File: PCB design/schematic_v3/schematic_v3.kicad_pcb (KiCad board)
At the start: 4 copper layers, 108 parts, among them IC1 LAN9252, J1 Conn_01x04_Pin, J2 connection_moteur, J3 Conn_01x05_Pin, J4 Conn_01x03_Pin, J5 Conn_01x02_Pin, Q1 AO3400A, U1 HX1188NL, U2 SP3485CN, U3 24FC512-I/ST, U4 LMR14030SQDPRTQ1, U5 STM32F446RETx, U7 AP63203WU, Y1 25MHz, Y2 8MHz

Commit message: pcb updated
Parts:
- removed C50, C51, C57: 100n, Capacitor_SMD:C_0603_1608Metric
- removed C52: 270p, Capacitor_SMD:C_0603_1608Metric
- removed C53, C55: 27u, Capacitor_SMD:C_1206_3216Metric
- removed C56: 10u, Capacitor_SMD:C_1206_3216Metric
- removed C58, C59: 22u, Capacitor_SMD:C_1206_3216Metric
- removed L3: 6.8u, Inductor_SMD:L_Bourns-SRN4018
- removed U7: AP63203WU, Package_TO_SOT_SMD:TSOT-23-6
- added C23: 18p, Capacitor_SMD:C_0603_1608Metric, F.Cu at (160.4, 90.1)
- added C24: 100n, Capacitor_SMD:C_0603_1608Metric, F.Cu at (149.4, 106.0)
- added C25: 100n, Capacitor_SMD:C_0603_1608Metric, F.Cu at (159.1, 109.5)
- added C31: 100n, Capacitor_SMD:C_0603_1608Metric, F.Cu at (142.1, 105.9)
- added C32: 20p, Capacitor_SMD:C_0603_1608Metric, F.Cu at (135.9, 105.9)
- added C34: 100n, Capacitor_SMD:C_0603_1608Metric, B.Cu at (176.7, 102.3)
- added C36: 1u, Capacitor_SMD:C_0603_1608Metric, F.Cu at (133.8, 89.5)
- added C37: 4.7u, Capacitor_SMD:C_0603_1608Metric, F.Cu at (147.2, 95.6)
- added C49: 22u, Capacitor_SMD:C_1206_3216Metric, B.Cu at (164.6, 83.0)
- added F1: 2920L150_60MR, footprints:2920L150_60MR, B.Cu at (176.4, 110.1)
- added H1: MountingHole, MountingHole:MountingHole_3.2mm_M3_Pad_Via, F.Cu at (127.5, 80.2)
- added H2: MountingHole, MountingHole:MountingHole_3.2mm_M3_Pad_Via, F.Cu at (186.5, 115.2)
- added H3: MountingHole, MountingHole:MountingHole_3.2mm_M3_Pad_Via, F.Cu at (127.5, 115.2)
- added H4: MountingHole, MountingHole:MountingHole_3.2mm_M3_Pad_Via, F.Cu at (186.5, 80.2)
- added L2: 6.8u, Inductor_SMD:L_Bourns-SRN4018, B.Cu at (167.5, 89.5)
- added U6: AP63203WU, Package_TO_SOT_SMD:TSOT-23-6, B.Cu at (173.9, 88.5)
- C1, C11, C13, C15, C16, C17, C21, C28, C35: value 0.1u -> 100n
- C10: value 47u -> 1n; footprint Capacitor_SMD:CP_Elec_5x5.4 -> Capacitor_SMD:C_0603_1608Metric; moved to F.Cu
- C18: value 47u -> 1u; footprint Capacitor_SMD:CP_Elec_5x5.4 -> Capacitor_SMD:C_0603_1608Metric; moved to F.Cu
- C20: value 1u -> 100n
- C22: value 0.1u -> 18p
- C26: value 18p -> 47u; footprint Capacitor_SMD:C_0603_1608Metric -> Capacitor_SMD:CP_Elec_5x5.4; moved to B.Cu
- C27: value 18p -> 100n
- C30: value 0.1u -> 100n; footprint Capacitor_SMD:C_0603_1608Metric -> Capacitor_SMD:C_1206_3216Metric; moved to B.Cu
- C33: value 0.1u -> 20p
- C38: footprint Capacitor_SMD:C_1206_3216Metric -> Capacitor_SMD:C_0603_1608Metric; moved to F.Cu
- C39: value 100n -> 10u; footprint Capacitor_SMD:C_0603_1608Metric -> Capacitor_SMD:C_1206_3216Metric; moved to B.Cu
- C40, C41: value 20p -> 100n
- C44: value 1u -> 270p; moved to B.Cu
- C45: value 4.7u -> 100n; moved to B.Cu
- C46, C48: value 100n -> 27u; footprint Capacitor_SMD:C_0603_1608Metric -> Capacitor_SMD:C_1206_3216Metric; moved to B.Cu
- C47: value 100n -> 22u; footprint Capacitor_SMD:C_0603_1608Metric -> Capacitor_SMD:C_1206_3216Metric; moved to B.Cu
- C5: value 10p -> 100n; moved to B.Cu
- C6: value 0.1u -> 10p; moved to F.Cu
- C8: moved to F.Cu
- C9: value 1n -> 47u; footprint Capacitor_SMD:C_0603_1608Metric -> Capacitor_SMD:CP_Elec_5x5.4
- J2: value connection_moteur -> Conn_01x02_Pin; footprint Connector_JST:JST_EH_B4B-EH-A_1x04_P2.50mm_Vertical -> Connector_JST:JST_EH_B2B-EH-A_1x02_P2.50mm_Vertical
- J3: value Conn_01x05_Pin -> connection_moteur; footprint Connector_PinHeader_1.27mm:PinHeader_1x05_P1.27mm_Vertical -> Connector_JST:JST_EH_B4B-EH-A_1x04_P2.50mm_Vertical
- J4: value Conn_01x03_Pin -> Conn_01x05_Pin; footprint Connector_PinHeader_1.27mm:PinHeader_1x03_P1.27mm_Vertical -> Connector_PinHeader_1.27mm:PinHeader_1x05_P1.27mm_Vertical
- J5: value Conn_01x02_Pin -> Conn_01x03_Pin; footprint Connector_JST:JST_EH_B2B-EH-A_1x02_P2.50mm_Vertical -> Connector_JST:JST_EH_B3B-EH-A_1x03_P2.50mm_Vertical; moved to F.Cu
- R1: value 49.9 -> 47k; moved to B.Cu
- R16: value 12.1k -> 12k
- R2: value 47k -> 49.9; moved to F.Cu
- S1: value TS40-66-43-BK-260-SMT-TR -> B3U-1100PM; footprint footprints:TS40-66-43-BK-260-SMT-TR -> footprints:B3U1100PM
- U1: value HX1188NL -> SP3485CN; footprint footprints:HX1188NL -> Package_SO:SOIC-8_3.9x4.9mm_P1.27mm; moved to B.Cu
- U2: value SP3485CN -> HX1188NL; footprint Package_SO:SOIC-8_3.9x4.9mm_P1.27mm -> footprints:HX1188NL; moved to F.Cu
- moved Q1 100.9 mm to (132.5, 105.4), turned to -90 degrees
- moved R14 98.1 mm to (132.5, 100.8), turned to 180 degrees
- moved R13 98.1 mm to (132.5, 102.3), turned to 0 degrees
- moved J5 98.0 mm to (134.8, 116.2), turned to 0 degrees
- moved C38 92.0 mm to (149.5, 102.5), turned to 180 degrees
- moved D1 91.7 mm to (138.1, 110.9), turned to 180 degrees
- moved R3 90.5 mm to (137.4, 96.5), turned to 180 degrees
- moved R10 86.6 mm to (148.0, 97.0), turned to 90 degrees
- moved R9 86.4 mm to (148.5, 99.7), turned to 180 degrees
- moved R8 85.8 mm to (146.0, 93.5), turned to 180 degrees
- moved D3 81.8 mm to (149.3, 110.9), turned to 180 degrees
- moved L1 79.1 mm to (162.1, 111.5), turned to -90 degrees
- moved J2 78.6 mm to (177.3, 116.2), turned to 0 degrees
- moved C18 74.7 mm to (165.6, 106.2), turned to 90 degrees
- moved R24 66.3 mm to (171.6, 93.8), turned to 90 degrees
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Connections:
- net Net-(IC1-RBIAS) renamed /RBIAS
- net Net-(IC1-VDD33BIAS) renamed /VDD33BIAS
- net Net-(Q1-G) renamed /GATE
- net Net-(U3-A0) renamed /AX
- net Net-(U4-PGOOD) renamed /PGOOD
- net Net-(U4-RT_SYNC) renamed /RT_SYNC
- net Net-(U5-BOOT0) renamed /BOOT0
- net Net-(U5-PA5) renamed /PA5
- net Net-(U5-PA6) renamed /PA6
- net Net-(U5-PA7) renamed /PA7
- C10 pad 1: +12V -> /CMT
- C18 pad 1: Net-(D2-K) -> /VDD33TXRX1
- C19 pad 1: /VDD33TXRX1 -> /VDD33TXRX2
- C20 pad 1: /VDD33TXRX2 -> /VDDCR
- C21 pad 1: /VDDCR -> +3.3V
- C22 pad 1: +3.3V -> GND
- C22 pad 2: GND -> Net-(C22-Pad2)
- C26 pad 1: GND -> /VIN
- C26 pad 2: Net-(C26-Pad2) -> GND
- C27 pad 1: GND -> /VDD12TX1
- C27 pad 2: /OSCO -> GND
- C28 pad 1: +3.3V -> /VDD12TX1
- C29 pad 1: Net-(D2-K) -> /VIN
- C30 pad 1: GND -> /VIN
- C30 pad 2: +3.3V -> GND
- C33 pad 1: /VDD12TX1 -> GND
- C33 pad 2: GND -> /PH1
- C35 pad 1: /VDD12TX1 -> GND
- C35 pad 2: GND -> /NRST
- C38 pad 1: Net-(D2-K) -> +3.3V
- C38 pad 2: GND -> /VDD19
- C39 pad 1: /AVDD -> +12V
- C40 pad 1: GND -> +3.3V
- C40 pad 2: Net-(U5-PH0) -> /VDD32
- C41 pad 1: GND -> +3.3V
- C41 pad 2: Net-(U5-PH1) -> /VDD48
- C42 pad 1: Net-(U4-SS) -> /BOOT
- C42 pad 2: GND -> /SW
- C43 pad 1: GND -> +3.3V
- C43 pad 2: /NRST -> /VDD64
- C44 pad 1: GND -> +12V
- C44 pad 2: +3.3V -> /FB
- C45 pad 1: Net-(U5-VCAP_1) -> /SW
- C45 pad 2: GND -> /BST
- C46 pad 1: +3.3V -> +12V
- C46 pad 2: Net-(C46-Pad2) -> GND
- C47 pad 2: Net-(C47-Pad2) -> GND
- C48 pad 1: +3.3V -> +12V
- C48 pad 2: Net-(C48-Pad2) -> GND
- C5 pad 1: /RXA_N -> +3.3V
- C6 pad 1: +3.3V -> /RXA_N
- C7 pad 1: Net-(U1-RCT) -> /TCT
- C9 pad 1: Net-(C9-Pad1) -> +12V
- D1 pad 1: Net-(D1-K) -> +12V
- D1 pad 2: +12V -> /DRAIN
- D2 pad 1: Net-(D2-K) -> /VIN
- D2 pad 2: +36V -> Net-(D2-A)
- D3 pad 1: Net-(D3-K) -> /SW
- J1 pad 1: Net-(J1-Pin_1) -> /RX_N
- J1 pad 2: Net-(J1-Pin_2) -> /RX_P
- J1 pad 3: Net-(J1-Pin_3) -> /TX_N
- J1 pad 4: Net-(J1-Pin_4) -> /TX_P
- J2 pad 1: Net-(D1-K) -> GND
- J2 pad 2: +12V -> +36V
- J3 pad 1: /SWDIO -> /DRAIN
- J3 pad 2: /SWCLK -> +12V
- J3 pad 3: GND -> /DATA+
- J3 pad 4: +3.3V -> /DATA-
- J4 pad 1: Net-(J4-Pin_1) -> /SWDIO
- J4 pad 2: Net-(J4-Pin_2) -> /SWCLK
- J4 pad 3: Net-(J4-Pin_3) -> GND
- J5 pad 1: GND -> /PA1
- J5 pad 2: +36V -> /PA0
- L1 pad 1: Net-(D3-K) -> /SW
- Q1 pad 3: Net-(D1-K) -> /DRAIN
- R1 pad 1: /VDD33TXRX1 -> GND
- R1 pad 2: /TXA_P -> /RS485_MODE
- R10 pad 1: Net-(J2-Pin_4) -> /DATA-
- R10 pad 2: Net-(J2-Pin_3) -> /DATA+
- R11 pad 1: Net-(C9-Pad1) -> /CMT
- R11 pad 2: Net-(R11-Pad2) -> /CMT1
- R12 pad 1: Net-(C9-Pad1) -> /CMT
- R12 pad 2: Net-(R12-Pad2) -> /CMT2
- R2 pad 1: GND -> /VDD33TXRX1
- R2 pad 2: /RS485_MODE -> /TXA_P
- R20 pad 2: Net-(C26-Pad2) -> Net-(C22-Pad2)
- R23 pad 1: Net-(D2-K) -> /VIN
- R28 pad 2: Net-(U4-FB) -> /FB
- R29 pad 1: Net-(U4-FB) -> /FB
- R3 pad 1: Net-(U2-DE) -> /DE/RE
- R7 pad 2: Net-(U1-RCT) -> /TCT
- R8 pad 1: Net-(J2-Pin_3) -> /DATA+
- R9 pad 2: Net-(J2-Pin_4) -> /DATA-
- S1 pad 1: GND -> /NRST
- S1 pad 3: /NRST -> GND
- U1 pad 1: /TXA_P -> /RO
- U1 pad 2: Net-(U1-RCT) -> /DE/RE
- U1 pad 3: /TXA_N -> /DE/RE
- U1 pad 4: unconnected-(U1-NC-Pad4) -> /DI
- U1 pad 5: unconnected-(U1-NC-Pad5) -> GND
- U1 pad 6: /RXA_P -> /DATA+
- U1 pad 7: Net-(U1-RCT) -> /DATA-
- U1 pad 8: /RXA_N -> +3.3V
- U2 pad 1: /RO -> /TXA_P
- U2 pad 2: Net-(U2-DE) -> /TCT
- U2 pad 3: Net-(U2-DE) -> /TXA_N
- U2 pad 4: /DI -> unconnected-(U2-NC-Pad4)
- U2 pad 5: GND -> unconnected-(U2-NC-Pad5)
- U2 pad 6: Net-(J2-Pin_3) -> /RXA_P
- U2 pad 7: Net-(J2-Pin_4) -> /TCT
- U2 pad 8: +3.3V -> /RXA_N
- U4 pad 1: Net-(U4-BOOT) -> /BOOT
- U4 pad 10: Net-(D3-K) -> /SW
- U4 pad 2: Net-(D2-K) -> /VIN
- U4 pad 3: Net-(D2-K) -> /VIN
- U4 pad 4: Net-(D2-K) -> /VIN
- U4 pad 6: Net-(U4-SS) -> /SS
- U4 pad 7: Net-(U4-FB) -> /FB
- U5 pad 14: Net-(J4-Pin_2) -> /PA0
- U5 pad 15: Net-(J4-Pin_3) -> /PA1
- U5 pad 19: Net-(C46-Pad2) -> /VDD19
- U5 pad 20: Net-(J4-Pin_1) -> /PA4
- U5 pad 30: Net-(U5-VCAP_1) -> /VCAP_1
- U5 pad 32: Net-(C47-Pad2) -> /VDD32
- U5 pad 48: Net-(C48-Pad2) -> /VDD48
- U5 pad 5: Net-(U5-PH0) -> /PH0
- U5 pad 6: Net-(U5-PH1) -> /PH1
- U5 pad 64: Net-(C51-Pad2) -> /VDD64
- Y1 pad 2: Net-(C26-Pad2) -> Net-(C22-Pad2)
- Y2 pad 1: Net-(U5-PH1) -> /PH1
- Y2 pad 2: Net-(U5-PH0) -> /PH0
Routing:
- net GND: track 0.00 -> 132.1 mm, vias 0 -> 78
- net +3.3V: track 0.00 -> 81.0 mm, vias 0 -> 31
- net /DRAIN: track 0.00 -> 80.6 mm
- net /DATA+: track 0.00 -> 72.4 mm
- net /DATA-: track 0.00 -> 58.0 mm
- net +12V: track 18.4 -> 60.0 mm, vias 0 -> 7
- net /RST#: track 0.00 -> 37.7 mm, vias 0 -> 2
- net /SCS#: track 0.00 -> 36.7 mm, vias 0 -> 2
- net /SW: track 0.00 -> 35.8 mm
- net /IRQ: track 0.00 -> 30.1 mm, vias 0 -> 2
- net /RXA_N: track 45.2 -> 15.5 mm, vias 0 -> 2
- net /PA0: track 0.00 -> 26.1 mm
- net /PA1: track 0.00 -> 26.0 mm
- net /PA4: track 0.00 -> 24.5 mm
- net /TX_N: track 0.00 -> 24.4 mm
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- added copper zone on B.Cu, net +12V
- added copper zone on In2.Cu, net +12V
- added copper zone on B.Cu, net +3.3V
- added copper zone on F.Cu, net +3.3V
- added copper zone on In2.Cu, net +3.3V
- added copper zone on B.Cu, net /GATE
- added copper zone on F.Cu, net /VDDCR
- added copper zone on B.Cu, net GND
- added copper zone on F.Cu, net GND
- added copper zone on In1.Cu, net GND
- added copper zone on In2.Cu, net GND
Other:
- board outline added: 67 x 43 mm
- board text added: "+3.3V"
- board text added: "+36V|GND"
- board text added: "ECAT"
- board text added: "GND"
- board text added: "GND|12V|D+|D-"
- board text added: "GPIO PINS"
- board text added: "Heemskerk Innovative Technology Robot Gripper Controller"
- board text added: "NRST"
- board text added: "PA0"
- board text added: "PA1"
- board text added: "PA4"
- board text added: "PWR"
- board text added: "RS485"
- board text added: "RX_N|RX_P|TX_N|TX_P"
- board text added: "SWCLK"
- board text added: "SWDIO"
- board text removed: "Module RS485"
- board text removed: "Zone EtherCAT (LAN9252)"
- board text removed: "Zone MCU"
- board text removed: "Zone d'alimentation"
- board text removed: "Zone entrée robot"

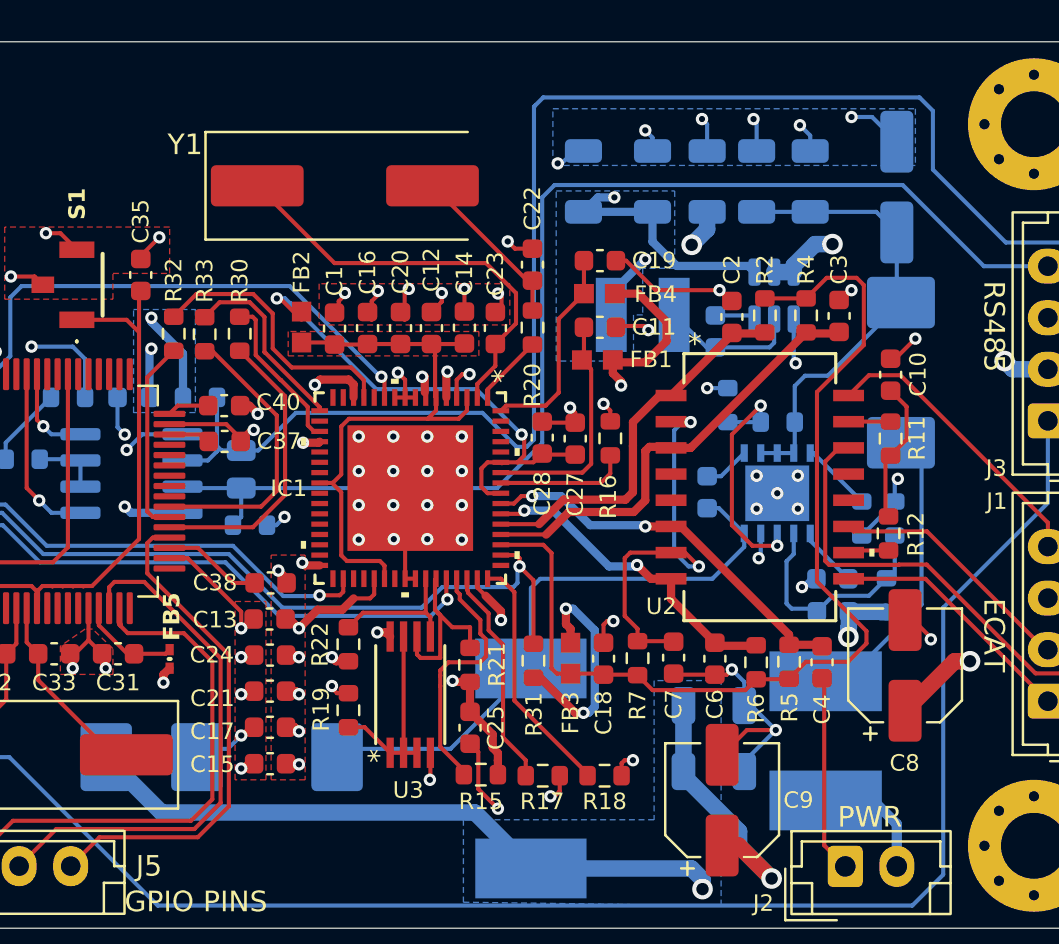
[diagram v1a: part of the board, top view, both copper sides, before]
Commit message: 1KHz ecat communication frequency done
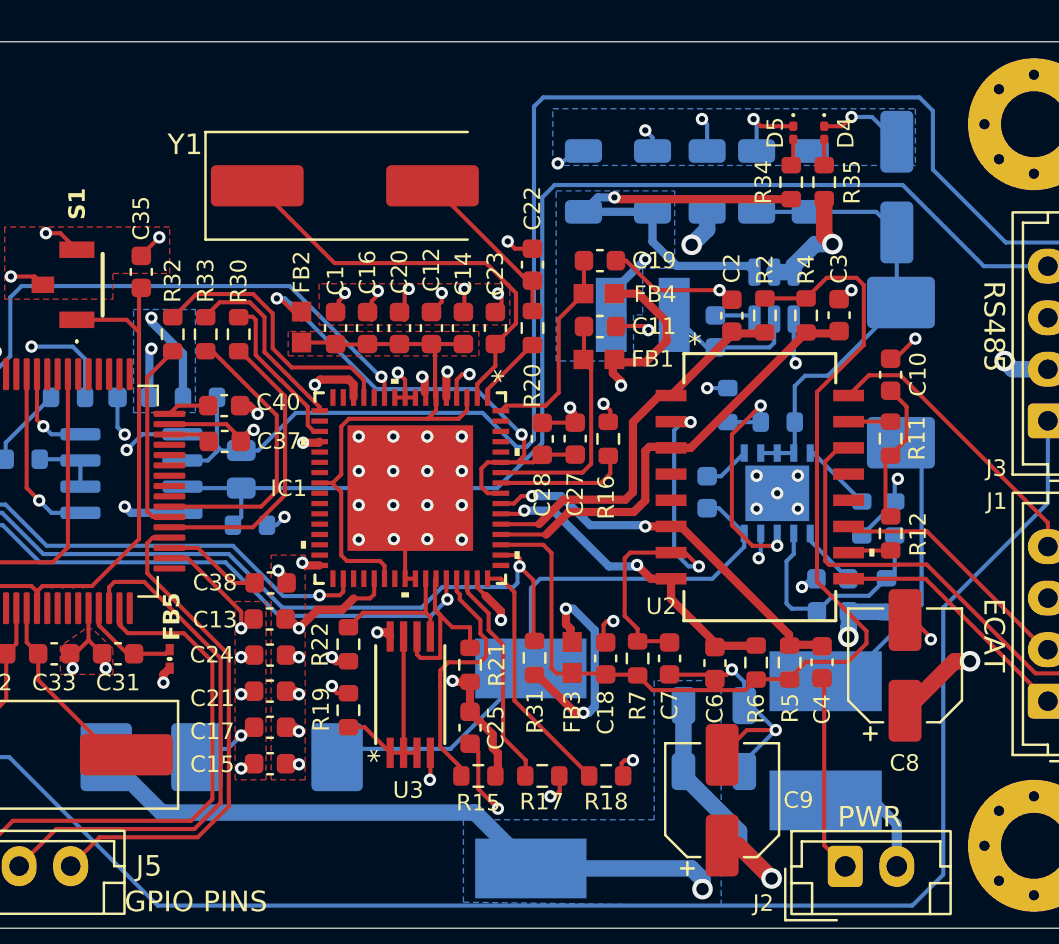
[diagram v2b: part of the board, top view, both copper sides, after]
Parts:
- added D4: LED_Small, LED_SMD:LED_0201_0603Metric, F.Cu at (176.3, 80.6)
- added D5: LED_Small, LED_SMD:LED_0201_0603Metric, F.Cu at (174.8, 80.6)
- added R34: 1k, Resistor_SMD:R_0603_1608Metric, F.Cu at (174.7, 83.0)
- added R35: 3.3k, Resistor_SMD:R_0603_1608Metric, F.Cu at (176.3, 83.0)
- moved C6 0.21 mm to (171.0, 106.4)
- moved C7 0.20 mm to (168.8, 106.1)
- moved C35 0.15 mm to (143.2, 87.4)
- moved R31 0.15 mm to (162.3, 106.1)
- moved R15 0.14 mm to (159.6, 111.8)
- moved C18 0.10 mm to (165.7, 106.1)
- moved R16 0.10 mm to (165.9, 95.5)
- moved R12 0.10 mm to (179.6, 100.1)
- moved FB3 0.09 mm to (164.1, 106.1)
- moved FB1 0.08 mm to (165.4, 91.6)
- moved R18 0.08 mm to (165.8, 111.8)
- moved C2 0.06 mm to (171.8, 89.5)
- moved C28 0.06 mm to (162.7, 95.5)
- moved R32 0.06 mm to (144.7, 90.4)
- moved C1 0.06 mm to (152.6, 90.1)
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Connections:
- C42 pad 2: /SW -> Net-(D3-K)
- D3 pad 1: /SW -> Net-(D3-K)
- L1 pad 1: /SW -> Net-(D3-K)
- U4 pad 10: /SW -> Net-(D3-K)
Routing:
- net /SW: track 35.8 -> 6.75 mm
- net Net-(D3-K): track 0.00 -> 29.1 mm
- net +3.3V: track 81.0 -> 89.7 mm
- net +12V: track 60.0 -> 62.4 mm
- net GND: track 132.1 -> 134.2 mm, vias 78 -> 77
- net Net-(D5-A): track 0.00 -> 1.25 mm
- net Net-(D4-A): track 0.00 -> 1.25 mm

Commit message: PCB ordered
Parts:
- removed Q1: AO3400A, Package_TO_SOT_SMD:SOT-23
- removed U2: HX1188NL, footprints:HX1188NL
- removed Y1: 25MHz, Crystal:Crystal_SMD_HC49-SD
- added C50: 10u, Capacitor_SMD:C_1206_3216Metric, B.Cu at (175.7, 88.6)
- added C51: 56p, Capacitor_SMD:C_0603_1608Metric, B.Cu at (168.7, 84.8)
- added D6: LED_Small, LED_SMD:LED_0603_1608Metric, F.Cu at (147.4, 98.7)
- added D7: LED_Small, LED_SMD:LED_0603_1608Metric, F.Cu at (132.1, 93.1)
- added D8: PRTR5V0U2X, Package_TO_SOT_SMD:SOT-143, F.Cu at (144.6, 116.1)
- added IC2: SON50P300X300X100-11N-D, footprints:MP5000ADQ-LF-Z, B.Cu at (171.8, 83.0)
- added R36: 1k, Resistor_SMD:R_0603_1608Metric, F.Cu at (131.4, 89.3)
- added R37: 10k, Resistor_SMD:R_0603_1608Metric, F.Cu at (135.5, 86.4)
- added R38: 1k, Resistor_SMD:R_0603_1608Metric, F.Cu at (147.3, 97.1)
- added R39: 1k, Resistor_SMD:R_0603_1608Metric, F.Cu at (132.6, 91.6)
- added R40: 1k, Resistor_SMD:R_0603_1608Metric, F.Cu at (140.2, 113.2)
- added R41: 1k, Resistor_SMD:R_0603_1608Metric, F.Cu at (136.5, 112.4)
- added R42: 1k, Resistor_SMD:R_0603_1608Metric, F.Cu at (134.9, 112.4)
- added R43: 10k, Resistor_SMD:R_0603_1608Metric, F.Cu at (142.9, 109.8)
- added R44: 10k, Resistor_SMD:R_0603_1608Metric, F.Cu at (144.5, 109.8)
- added R45: 10k, Resistor_SMD:R_0603_1608Metric, F.Cu at (146.1, 109.8)
- added R46: 100, Resistor_SMD:R_0603_1608Metric, F.Cu at (178.4, 85.4)
- added R47: 100, Resistor_SMD:R_0603_1608Metric, F.Cu at (165.8, 82.0)
- added S2: B3U-1100PM, footprints:B3U1100PM, F.Cu at (128.1, 94.9)
- added T1: 7490100110A, footprints:7490100110A, F.Cu at (176.0, 98.5)
- added TP1: TestPoint, TestPoint:TestPoint_Pad_D1.0mm, F.Cu at (176.0, 108.4)
- added TP2: TestPoint, TestPoint:TestPoint_Pad_D1.0mm, F.Cu at (180.2, 83.6)
- added TP3: TestPoint, TestPoint:TestPoint_Pad_D1.0mm, F.Cu at (165.6, 79.4)
- added TP4: TestPoint, TestPoint:TestPoint_Pad_D1.0mm, F.Cu at (146.2, 83.0)
- added TP5: TestPoint, TestPoint:TestPoint_Pad_D1.0mm, B.Cu at (130.2, 94.0)
- added TP6: TestPoint, TestPoint:TestPoint_Pad_D1.0mm, B.Cu at (131.7, 102.9)
- added TP7: TestPoint, TestPoint:TestPoint_Pad_D1.0mm, B.Cu at (128.3, 97.8)
- added TP8: TestPoint, TestPoint:TestPoint_Pad_D1.0mm, B.Cu at (162.3, 81.1)
- added TP9: TestPoint, TestPoint:TestPoint_Pad_D1.0mm, F.Cu at (157.4, 80.4)
- added U7: MAX3485, Package_SO:SOIC-8_3.9x4.9mm_P1.27mm, B.Cu at (142.8, 97.2)
- added Y3: ABM3-25.000MHZ-D2Y-T, footprints:ABM3-25.000MHZ-D2Y-T, F.Cu at (162.0, 88.2)
- C32, C33: value 20p -> 27p
- C46, C48: footprint Capacitor_SMD:C_1206_3216Metric -> Capacitor_SMD:C_Elec_4x5.8
- C8: value 47u -> 10u
- C9: value 47u -> 1u; footprint Capacitor_SMD:CP_Elec_5x5.4 -> Capacitor_SMD:CP_Elec_4x5.4
- D1, D2: value B340 -> PMEG3020EJ; footprint Diode_SMD:D_SMC -> Diode_SMD:D_SOD-323F
- D3: value B340 -> PRTR5V0U2X; footprint Diode_SMD:D_SMC -> Package_TO_SOT_SMD:SOT-143; moved to F.Cu
- D4, D5: footprint LED_SMD:LED_0201_0603Metric -> LED_SMD:LED_0603_1608Metric
- R14: value 10k -> 100; moved to F.Cu
- R16: value 12k -> 12.1k
- R21, R22: value 2k -> 1k
- U1: value SP3485CN -> SN74LVC3G17DCTRE4; footprint Package_SO:SOIC-8_3.9x4.9mm_P1.27mm -> footprints:SN74LVC3G17DCTRE4; moved to F.Cu
- Y2: value 8MHz -> ABM3-20.000MHZ-D2Y-T; footprint Crystal:Crystal_SMD_HC49-SD -> footprints:ABM3-20.000MHZ-D2Y-T
- moved H3 68.6 mm to (186.5, 80.2), turned to 0 degrees
- moved H2 59.0 mm to (127.5, 115.2), turned to 0 degrees
- moved D1 44.9 mm to (182.5, 104.0), turned to -90 degrees
- moved R13 44.9 mm to (171.7, 80.4)
- moved R14 44.5 mm to (175.8, 111.2), turned to -90 degrees
- moved H4 35.0 mm to (186.5, 115.2), turned to 0 degrees
- moved D2 19.4 mm to (163.4, 102.1), turned to 180 degrees
- moved U1 18.9 mm to (148.1, 115.3), turned to 90 degrees
- moved R4 17.3 mm to (163.4, 101.9), turned to 90 degrees
- moved C1 16.3 mm to (152.0, 106.4), turned to 90 degrees
- moved C3 16.3 mm to (164.2, 99.5), turned to 0 degrees
- moved C30 16.2 mm to (180.9, 97.2), turned to 180 degrees
- moved D3 16.2 mm to (133.2, 109.3), turned to 90 degrees
- moved C29 13.0 mm to (180.9, 94.9), turned to 180 degrees
- moved D5 11.6 mm to (163.2, 80.0)
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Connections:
- net /TCT renamed /RCT
- C10 pad 2: GND -> GNDREF
- C42 pad 2: Net-(D3-K) -> Net-(D2-K)
- D1 pad 1: +12V -> /VIN
- D1 pad 2: /DRAIN -> Net-(D1-A)
- D2 pad 1: /VIN -> Net-(D2-K)
- D2 pad 2: Net-(D2-A) -> GND
- D3 pad 1: Net-(D3-K) -> GND
- D3 pad 2: GND -> Net-(D3-I/O1)
- F1 pad 2: Net-(D2-A) -> Net-(D1-A)
- J3 pad 1: /DRAIN -> GND
- J3 pad 2: +12V -> Net-(J3-Pin_2)
- J5 pad 1: /PA1 -> Net-(J5-Pin_1)
- J5 pad 2: /PA0 -> Net-(J5-Pin_2)
- J5 pad 3: /PA4 -> Net-(J5-Pin_3)
- L1 pad 1: Net-(D3-K) -> Net-(D2-K)
- R13 pad 1: /GATE -> Net-(IC2-I-LIMIT)
- R13 pad 2: /ALIM_MOTOR -> Net-(IC2-SOURCE_1)
- R14 pad 1: GND -> Net-(R14-Pad1)
- R14 pad 2: /GATE -> +36V
- U1 pad 1: /RO -> Net-(D8-I/O1)
- U1 pad 2: /DE/RE -> /PA4
- U1 pad 3: /DE/RE -> Net-(D8-I/O2)
- U1 pad 4: /DI -> GND
- U1 pad 5: GND -> /PA0
- U1 pad 6: /DATA+ -> Net-(D3-I/O1)
- U1 pad 7: /DATA- -> /PA1
- U4 pad 10: Net-(D3-K) -> Net-(D2-K)
- U5 pad 29: unconnected-(U5-PB10-Pad29) -> /PB10
- U5 pad 50: unconnected-(U5-PA15-Pad50) -> /PA15
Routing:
- net /DRAIN: track 80.6 -> 0.00 mm
- net Net-(D3-K): track 29.1 -> 0.00 mm
- net +12V: track 62.4 -> 39.7 mm, vias 7 -> 14
- net /VDD33TXRX1: track 49.5 -> 27.5 mm
- net /ALIM_MOTOR: track 15.4 -> 37.4 mm
- net Net-(D3-I/O1): track 0.00 -> 17.8 mm
- net Net-(D8-I/O2): track 0.00 -> 16.7 mm
- net /DATA+: track 72.4 -> 57.1 mm
- net Net-(D2-A): track 14.5 -> 0.00 mm
- net /TX_N: track 24.4 -> 10.8 mm
- net +3.3V: track 89.7 -> 103.2 mm, vias 31 -> 37
- net Net-(D2-K): track 0.00 -> 13.1 mm
- net Net-(J3-Pin_2): track 0.00 -> 12.9 mm
- net /SWCLK: track 3.59 -> 16.3 mm
- net /OSCO: track 20.6 -> 10.9 mm
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- added copper zone on F.Cu, net +12V
- added copper zone on B.Cu, net /VIN
- added copper zone on In1.Cu, net GNDREF
- removed copper zone on B.Cu, net /GATE
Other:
- board text added: "+12V"
- board text added: "+36V"
- board text added: "ALIM_MOTOR"
- board text added: "IRQ"
- board text added: "RST#"
- board text added: "SYNC0"
- board text removed: "GPIO PINS"
